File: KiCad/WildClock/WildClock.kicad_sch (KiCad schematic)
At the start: 35 parts, among them J1 UART, Q1 CA1, Q2 CA2, Q3 CA3, Q4 CA4, Q5 CAL, SW1 ButtonUp, SW2 ButtonDown, SW3 ButtonOK, U1 ESP32-C3-MINI-1, U2 LTC-4627JR, U3 74HC595

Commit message: make all clearer and neu pcb
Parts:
- R1, R15, R2, R3, R4, R5: value 1kOhm -> 1k
- R10, R11, R12, R13, R14, R7, R8, R9: value 150Ohm -> 150
- R16, R6: value 10kOhm -> 10k
- U2: value LTC-4627JR -> 7Segment
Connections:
- net +3.3V: now also BT1.1 (+), C1.2, C2.2, R15.2, U1.3 (3V3)
- net GND: now also BT1.2 (-), C1.1, C2.1, C3.1, U1.1 (GND), U1.2 (GND), U1.36 (GND), U1.37 (GND), U1.38 (GND), U1.39 (GND), U1.40 (GND), U1.41 (GND), U1.42 (GND), U1.43 (GND), U1.44 (GND), U1.45 (GND), U1.46 (GND), U1.47 (GND), U1.48 (GND), U1.49 (GND), U1.50 (GND), U1.51 (GND), U1.52 (GND), U1.53 (GND)
- net Q2: now reaches R2.1, U1.19 (GPIO5/ADC2_CH0)
- net BUZZ: now reaches BZ1.1 (-), U1.16 (GPIO10)
- net at R10.1: now also U2.3 (D); no longer U3.4 (QE)
- net at U2.5 (E): now also R11.1; no longer R10.2
- net CA1: now reaches Q1.3 (E), U2.1 (CA1)
- net at R7.1: now also U2.14 (A); no longer U3.7 (QH)
- net at U2.7 (DP): now also R14.1; no longer R7.2
- net at R13.1: now also U2.15 (G); no longer U3.1 (QB)
- net at U2.16 (B): now also R8.1; no longer R13.2
- net SWOK: now reaches R16.1, SW3.1, U1.5 (GPIO2/ADC1_CH2)
- net at U2.11 (F): now also R12.1; no longer R9.2
- net at U2.13 (C): now also R9.1; no longer R12.2
- net DP: now reaches R14.2
- net DP: now also U3.15 (QA); no longer U2.14 (A)
- net B: now reaches R8.2
- net B: now also U3.6 (QG); no longer U2.15 (G)
- net CA2: now reaches Q2.3 (E), U2.2 (CA2)
- net E: now reaches R11.2
- net E: now also U3.3 (QD); no longer U2.3 (D)
- net CAL: now reaches Q5.3 (E), U2.4 (CAL)
- net CA3: now reaches Q3.3 (E), U2.6 (CA3)
- net CA4: now reaches Q4.3 (E), U2.8 (CA4)
- net TXD0: now reaches J1.2 (Pin_2), U1.31 (GPIO21/U0TXD)
- net RXD0: now reaches J1.3 (Pin_3), U1.30 (GPIO20/U0RXD)
- net SRCLK: now reaches U1.27 (GPIO19/USB_D+), U3.11 (SRCLK)
- net RCLK: now reaches U1.26 (GPIO18/USB_D-), U3.12 (RCLK)
- net RCLK: no longer JP1.2 (B)
- net SER: now reaches U1.23 (GPIO9), U3.14 (SER)
- net SER: now also JP1.2 (B)
- net F: now reaches U3.2 (QC)
- net F: now also R12.2; no longer R12.1
- net C: now reaches U3.5 (QF)
- net C: now also R9.2; no longer R9.1
- net SWDOWN: now reaches SW2.1, U1.12 (GPIO0/ADC1_CH0/XTAL_32K_P)
- net SWUP: now reaches SW1.1, U1.13 (GPIO1/ADC1_CH1/XTAL_32K_N)
- net Q1: now reaches R1.1, U1.18 (GPIO4/ADC1_CH4)
- net Q3: now reaches R3.1
- net Q3: now also U1.21 (GPIO7); no longer U1.20 (GPIO6)
- net Q4: now reaches R4.1
- net Q4: now also R6.1, U1.22 (GPIO8); no longer U1.21 (GPIO7)
- net TILT: now reaches S1.2, U1.6 (GPIO3/ADC1_CH3)
- new net: C3.2, R15.1, U1.8 (EN/CHIP_PU)
- new net A: R7.2, U3.7 (QH)
- new net D: R10.2, U3.4 (QE)
- new net G: R13.2, U3.1 (QB)
- new net QL: R5.1, U1.20 (GPIO6)
- no-connect marks 0 -> 1
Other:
- note added: "7 Segment controll"
- note added: "Buttons"
- note added: "ESP Pinout"
- note added: "Interfaces"
- note added: "Output"
- note added: "Power Circuit"
- note added: "Sensor"
- moved on the sheet: BT1, BZ1, J1, JP1, Q1, Q2, Q3, Q4, Q5, S1, SW1, SW2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

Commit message: changed some footprints
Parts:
- removed Q1: CA1, Package_TO_SOT_THT:TO-92_Inline, symbol Transistor_BJT:BC547
- removed Q2: CA2, Package_TO_SOT_THT:TO-92_Inline, symbol Transistor_BJT:BC547
- removed Q3: CA3, Package_TO_SOT_THT:TO-92_Inline, symbol Transistor_BJT:BC547
- removed Q4: CA4, Package_TO_SOT_THT:TO-92_Inline, symbol Transistor_BJT:BC547
- removed Q5: CAL, Package_TO_SOT_THT:TO-92_Inline, symbol Transistor_BJT:BC547
- added Q1: CA1, Package_TO_SOT_SMD:SOT-23, symbol Transistor_BJT:MMBT3904
- added Q2: CA2, Package_TO_SOT_SMD:SOT-23, symbol Transistor_BJT:MMBT3904
- added Q3: CA3, Package_TO_SOT_SMD:SOT-23, symbol Transistor_BJT:MMBT3904
- added Q4: CA4, Package_TO_SOT_SMD:SOT-23, symbol Transistor_BJT:MMBT3904
- added Q5: CAL, Package_TO_SOT_SMD:SOT-23, symbol Transistor_BJT:MMBT3904
- SW1, SW2, SW3: footprint Button_Switch_THT:SW_PUSH_6mm -> Button_Switch_SMD:SW_Push_1P1T_NO_6x6mm_H9.5mm
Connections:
- net +3.3V: now also Q1.3 (C), Q2.3 (C), Q3.3 (C), Q4.3 (C), Q5.3 (C)
- net CA1: now also Q1.2 (E)
- net CA2: now also Q2.2 (E)
- net CA3: now also Q3.2 (E)
- net CA4: now also Q4.2 (E)
- net CAL: now also Q5.2 (E)
- net at R2.2: now also Q2.1 (B)
- net at R1.2: now also Q1.1 (B)
- net at R5.2: now also Q5.1 (B)
- net at R4.2: now also Q4.1 (B)
- net at R3.2: now also Q3.1 (B)
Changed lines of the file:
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@@
     (pin "2")
+  )
+  (symbol (lib_id "Transistor_BJT:MMBT3904") (at 31.75 104.14 270) (unit 1)
+    (in_bom yes) (on_board yes)
+    (property "Reference" "Q4" (id 0) (at 29.21 101.6 90))
+    (property "Value" "CA4" (id 1) (at 31.75 109.22 90))
+    (property "Footprint" "Package_TO_SOT_SMD:SOT-23" (id 2) (at 29.845 109.22 0)
+      (effects (font (size 1.27 1.27) italic) (justify left) hide)
+    )
+    (property "Datasheet" "https://www.onsemi.com/pub/Collateral/2N3903-D.PDF" (id 3) (at 31.75 104.14 0)
+      (effects (font (size 1.27 1.27)) (justify left) hide)
+    )
+    (pin "1")
+    (pin "2")
+    (pin "3")
   )
   (symbol (lib_id "power:GND") (at 153.67 107.95 90) (unit 1)
@@
     (pin "1")
   )
+  (symbol (lib_id "Transistor_BJT:MMBT3904") (at 31.75 63.5 270) (unit 1)
+    (in_bom yes) (on_board yes)
+    (property "Reference" "Q1" (id 0) (at 29.21 60.96 90))
+    (property "Value" "CA1" (id 1) (at 31.75 68.58 90))
+    (property "Footprint" "Package_TO_SOT_SMD:SOT-23" (id 2) (at 29.845 68.58 0)
+      (effects (font (size 1.27 1.27) italic) (justify left) hide)
+    )
+    (property "Datasheet" "https://www.onsemi.com/pub/Collateral/2N3903-D.PDF" (id 3) (at 31.75 63.5 0)
+      (effects (font (size 1.27 1.27)) (justify left) hide)
+    )
+    (pin "1")
+    (pin "2")
+    (pin "3")
+  )
   (symbol (lib_id "Device:Buzzer") (at 167.64 139.7 0) (mirror y) (unit 1)
     (in_bom yes) (on_board yes)
@@
     (pin "2")
   )
-  (symbol (lib_id "Transistor_BJT:BC547") (at 31.75 63.5 270) (unit 1)
-    (in_bom yes) (on_board yes)
-    (property "Reference" "Q1" (id 0) (at 29.21 60.96 90))
-    (property "Value" "CA1" (id 1) (at 31.75 68.58 90))
-    (property "Footprint" "Package_TO_SOT_THT:TO-92_Inline" (id 2) (at 29.845 68.58 0)
+  (symbol (lib_id "Transistor_BJT:MMBT3904") (at 31.75 116.84 270) (unit 1)
+    (in_bom yes) (on_board yes)
+    (property "Reference" "Q5" (id 0) (at 29.21 114.3 90))
+    (property "Value" "CAL" (id 1) (at 31.75 121.92 90))
+    (property "Footprint" "Package_TO_SOT_SMD:SOT-23" (id 2) (at 29.845 121.92 0)
       (effects (font (size 1.27 1.27) italic) (justify left) hide)
     )
-    (property "Datasheet" "https://www.onsemi.com/pub/Collateral/BC550-D.pdf" (id 3) (at 31.75 63.5 0)
+    (property "Datasheet" "https://www.onsemi.com/pub/Collateral/2N3903-D.PDF" (id 3) (at 31.75 116.84 0)
       (effects (font (size 1.27 1.27)) (justify left) hide)
     )
@@
     (property "Reference" "SW3" (id 0) (at 88.9 133.35 0))
     (property "Value" "ButtonOK" (id 1) (at 88.9 135.89 0))
-    (property "Footprint" "Button_Switch_THT:SW_PUSH_6mm" (id 2) (at 88.9 135.89 0)
+    (property "Footprint" "Button_Switch_SMD:SW_Push_1P1T_NO_6x6mm_H9.5mm" (id 2) (at 88.9 135.89 0)
       (effects (font (size 1.27 1.27)) hide)
     )
@@
     (pin "4")
   )
-  (symbol (lib_id "Transistor_BJT:BC547") (at 31.75 116.84 270) (unit 1)
-    (in_bom yes) (on_board yes)
-    (property "Reference" "Q5" (id 0) (at 29.21 114.3 90))
-    (property "Value" "CAL" (id 1) (at 31.75 121.92 90))
-    (property "Footprint" "Package_TO_SOT_THT:TO-92_Inline" (id 2) (at 29.845 121.92 0)
+  (symbol (lib_id "Transistor_BJT:MMBT3904") (at 31.75 91.44 270) (unit 1)
+    (in_bom yes) (on_board yes)
+    (property "Reference" "Q3" (id 0) (at 29.21 88.9 90))
+    (property "Value" "CA3" (id 1) (at 31.75 96.52 90))
+    (property "Footprint" "Package_TO_SOT_SMD:SOT-23" (id 2) (at 29.845 96.52 0)
       (effects (font (size 1.27 1.27) italic) (justify left) hide)
     )
-    (property "Datasheet" "https://www.onsemi.com/pub/Collateral/BC550-D.pdf" (id 3) (at 31.75 116.84 0)
+    (property "Datasheet" "https://www.onsemi.com/pub/Collateral/2N3903-D.PDF" (id 3) (at 31.75 91.44 0)
+      (effects (font (size 1.27 1.27)) (justify left) hide)
+    )
+    (pin "1")
+    (pin "2")
+    (pin "3")
+  )
+  (symbol (lib_id "Transistor_BJT:MMBT3904") (at 31.75 77.47 270) (unit 1)
+    (in_bom yes) (on_board yes)
+    (property "Reference" "Q2" (id 0) (at 29.21 74.93 90))
+    (property "Value" "CA2" (id 1) (at 31.75 82.55 90))
+    (property "Footprint" "Package_TO_SOT_SMD:SOT-23" (id 2) (at 29.845 82.55 0)
+      (effects (font (size 1.27 1.27) italic) (justify left) hide)
+    )
+    (property "Datasheet" "https://www.onsemi.com/pub/Collateral/2N3903-D.PDF" (id 3) (at 31.75 77.47 0)
       (effects (font (size 1.27 1.27)) (justify left) hide)
     )
@@
     (pin "2")
   )
-  (symbol (lib_id "Transistor_BJT:BC547") (at 31.75 91.44 270) (unit 1)
-    (in_bom yes) (on_board yes)
-    (property "Reference" "Q3" (id 0) (at 29.21 88.9 90))
-    (property "Value" "CA3" (id 1) (at 31.75 96.52 90))
-    (property "Footprint" "Package_TO_SOT_THT:TO-92_Inline" (id 2) (at 29.845 96.52 0)
-      (effects (font (size 1.27 1.27) italic) (justify left) hide)
-    )
-    (property "Datasheet" "https://www.onsemi.com/pub/Collateral/BC550-D.pdf" (id 3) (at 31.75 91.44 0)
-      (effects (font (size 1.27 1.27)) (justify left) hide)
-    )
-    (pin "1")
-    (pin "2")
-    (pin "3")
-  )
-  (symbol (lib_id "Transistor_BJT:BC547") (at 31.75 77.47 270) (unit 1)
-    (in_bom yes) (on_board yes)
-    (property "Reference" "Q2" (id 0) (at 29.21 74.93 90))
-    (property "Value" "CA2" (id 1) (at 31.75 82.55 90))
-    (property "Footprint" "Package_TO_SOT_THT:TO-92_Inline" (id 2) (at 29.845 82.55 0)
-      (effects (font (size 1.27 1.27) italic) (justify left) hide)
-    )
-    (property "Datasheet" "https://www.onsemi.com/pub/Collateral/BC550-D.pdf" (id 3) (at 31.75 77.47 0)
-      (effects (font (size 1.27 1.27)) (justify left) hide)
-    )
-    (pin "1")
-    (pin "2")
-    (pin "3")
-  )
   (symbol (lib_id "Device:R") (at 121.92 57.15 270) (unit 1)
     (in_bom yes) (on_board yes)
@@
     (pin "1")
   )
-  (symbol (lib_id "Transistor_BJT:BC547") (at 31.75 104.14 270) (unit 1)
-    (in_bom yes) (on_board yes)
-    (property "Reference" "Q4" (id 0) (at 29.21 101.6 90))
-    (property "Value" "CA4" (id 1) (at 31.75 109.22 90))
-    (property "Footprint" "Package_TO_SOT_THT:TO-92_Inline" (id 2) (at 29.845 109.22 0)
-      (effects (font (size 1.27 1.27) italic) (justify left) hide)
-    )
-    (property "Datasheet" "https://www.onsemi.com/pub/Collateral/BC550-D.pdf" (id 3) (at 31.75 104.14 0)
-      (effects (font (size 1.27 1.27)) (justify left) hide)
-    )
-    (pin "1")
-    (pin "2")
-    (pin "3")
-  )
   (symbol (lib_id "Switch:SW_Push") (at 27.94 140.97 0) (unit 1)
     (in_bom yes) (on_board yes)
     (property "Reference" "SW1" (id 0) (at 27.94 133.35 0))
     (property "Value" "ButtonUp" (id 1) (at 27.94 135.89 0))
-    (property "Footprint" "Button_Switch_THT:SW_PUSH_6mm" (id 2) (at 27.94 135.89 0)
+    (property "Footprint" "Button_Switch_SMD:SW_Push_1P1T_NO_6x6mm_H9.5mm" (id 2) (at 27.94 135.89 0)
       (effects (font (size 1.27 1.27)) hide)
     )
@@
     (property "Reference" "SW2" (id 0) (at 59.69 133.35 0))
     (property "Value" "ButtonDown" (id 1) (at 59.69 135.89 0))
-    (property "Footprint" "Button_Switch_THT:SW_PUSH_6mm" (id 2) (at 59.69 135.89 0)
+    (property "Footprint" "Button_Switch_SMD:SW_Push_1P1T_NO_6x6mm_H9.5mm" (id 2) (at 59.69 135.89 0)
       (effects (font (size 1.27 1.27)) hide)
     )
@@
       (reference "JP1") (unit 1) (value "Jumper_BOOT") (footprint "Connector_PinHeader_1.00mm:PinHeader_1x02_P1.00mm_Vertical")
     )
-    (path "/19149466-093f-494c-ad9e-63c53e92a41b"
-      (reference "Q1") (unit 1) (value "CA1") (footprint "Package_TO_SOT_THT:TO-92_Inline")
-    )
-    (path "/979b9bbf-6e1a-42d0-8fea-eb42374f2a80"
-      (reference "Q2") (unit 1) (value "CA2") (footprint "Package_TO_SOT_THT:TO-92_Inline")
-    )
-    (path "/8d0c18fa-e270-4d4a-a033-ec5a68a676e3"
-      (reference "Q3") (unit 1) (value "CA3") (footprint "Package_TO_SOT_THT:TO-92_Inline")
-    )
-    (path "/9ddf3c1f-7b3f-445c-8f18-ffb30090172f"
-      (reference "Q4") (unit 1) (value "CA4") (footprint "Package_TO_SOT_THT:TO-92_Inline")
-    )
-    (path "/4528a993-2673-4497-ae4f-06a4d5527096"
-      (reference "Q5") (unit 1) (value "CAL") (footprint "Package_TO_SOT_THT:TO-92_Inline")
+    (path "/076122f5-8a6d-41b4-9ff2-bda110edd813"
+      (reference "Q1") (unit 1) (value "CA1") (footprint "Package_TO_SOT_SMD:SOT-23")
+    )
+    (path "/44421386-2f43-4f34-ae8c-25366510c86b"
+      (reference "Q2") (unit 1) (value "CA2") (footprint "Package_TO_SOT_SMD:SOT-23")
+    )
+    (path "/3bbfdfa1-1f8e-4402-afb4-0c680a8663bf"
+      (reference "Q3") (unit 1) (value "CA3") (footprint "Package_TO_SOT_SMD:SOT-23")
+    )
+    (path "/0360746b-949e-4ad8-99c4-b4de53620631"
+      (reference "Q4") (unit 1) (value "CA4") (footprint "Package_TO_SOT_SMD:SOT-23")
+    )
+    (path "/161405ae-9068-4ac5-9c97-4db296fcbd48"
+      (reference "Q5") (unit 1) (value "CAL") (footprint "Package_TO_SOT_SMD:SOT-23")
     )
     (path "/f526df69-e0a2-4d6a-a448-2fc1af5fcd15"
@@
     )
     (path "/a0f7afd9-e1a0-4493-927b-f858c896c28f"
-      (reference "SW1") (unit 1) (value "ButtonUp") (footprint "Button_Switch_THT:SW_PUSH_6mm")
+      (reference "SW1") (unit 1) (value "ButtonUp") (footprint "Button_Switch_SMD:SW_Push_1P1T_NO_6x6mm_H9.5mm")
     )
     (path "/b1a991f1-4115-440b-91b7-23f9271c3989"
-      (reference "SW2") (unit 1) (value "ButtonDown") (footprint "Button_Switch_THT:SW_PUSH_6mm")
+      (reference "SW2") (unit 1) (value "ButtonDown") (footprint "Button_Switch_SMD:SW_Push_1P1T_NO_6x6mm_H9.5mm")
     )
     (path "/1eaec3da-e070-4c8f-a604-d4f168f6fdf4"
-      (reference "SW3") (unit 1) (value "ButtonOK") (footprint "Button_Switch_THT:SW_PUSH_6mm")
+      (reference "SW3") (unit 1) (value "ButtonOK") (footprint "Button_Switch_SMD:SW_Push_1P1T_NO_6x6mm_H9.5mm")
     )
     (path "/59553d1f-db58-4ebb-922c-4e1354cf99f4"

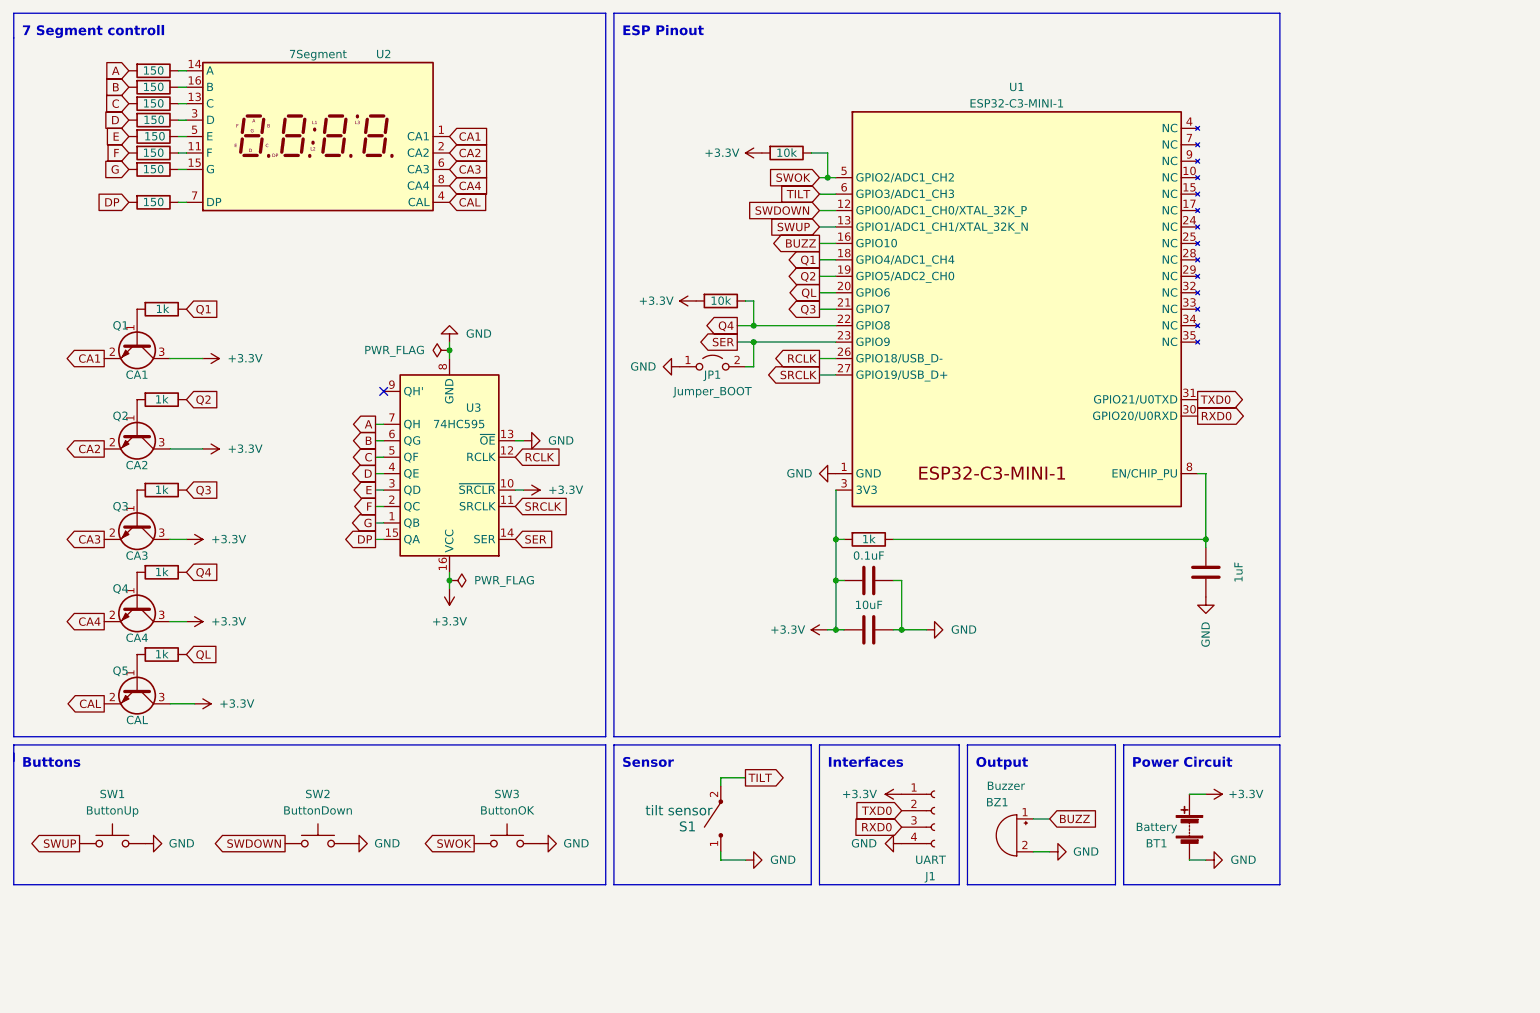
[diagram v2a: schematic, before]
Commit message: start updating footprints to match jlcpcb
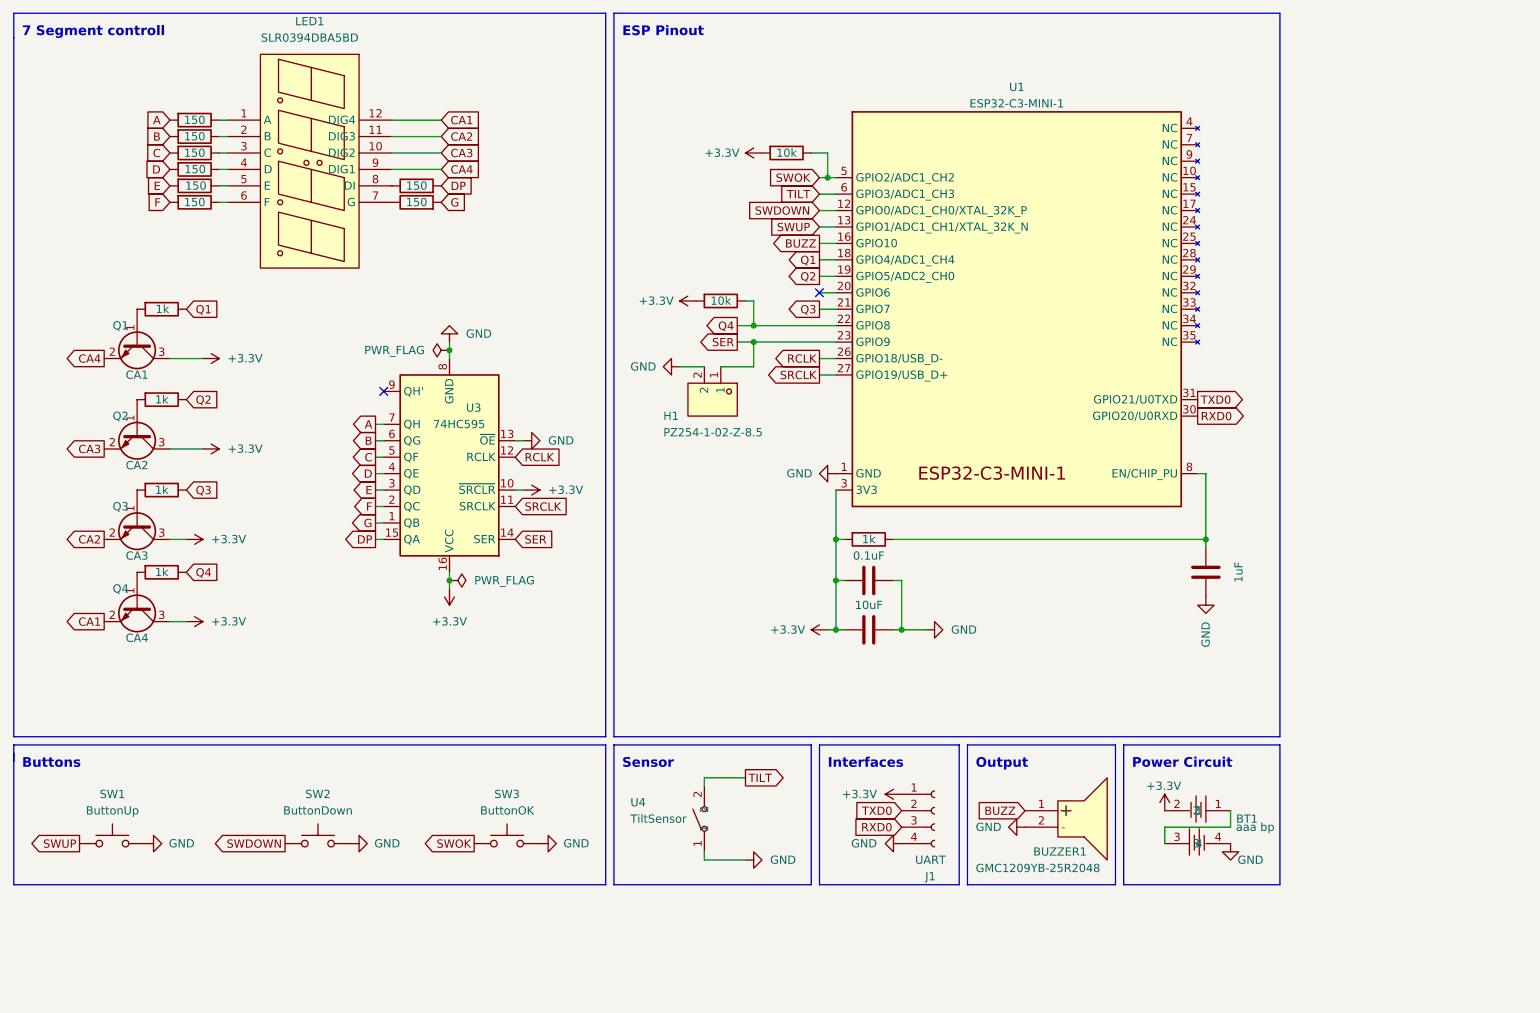
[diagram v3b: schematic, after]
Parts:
- removed BT1: Battery, Battery:BatteryHolder_Keystone_2462_2xAA, symbol Device:Battery
- removed BZ1: Buzzer, Buzzer_Beeper:Buzzer_12x9.5RM7.6, symbol Device:Buzzer
- removed JP1: Jumper_BOOT, Connector_PinHeader_1.00mm:PinHeader_1x02_P1.00mm_Vertical, symbol Jumper:Jumper_2_Open
- removed Q5: CAL, Package_TO_SOT_SMD:SOT-23, symbol Transistor_BJT:MMBT3904
- removed R5: 1k, Resistor_SMD:R_0805_2012Metric, symbol Device:R
- removed S1: tilt sensor, digikey-footprints:Tilt_Switch_RB-220-07A_R, symbol dk_Motion-Sensors-Tilt-Switches:RB-220-07A_R
- removed U2: 7Segment, Display_7Segment:LTC-4627Jx, symbol Display_Character:LTC-4627JR
- added BT1: aaa bp, easyeda2kicad:BAT-SMD_BH-AAA-B5AA001, symbol easyeda2kicad:BH-AAA-B5AA001
- added BUZZER1: GMC1209YB-25R2048, easyeda2kicad:BUZ-TH_BD12.0-P6.50-D0.6-FD, symbol easyeda2kicad:GMC1209YB-25R2048
- added H1: PZ254-1-02-Z-8.5, easyeda2kicad:HDR-TH_2P-P2.54-V-M, symbol easyeda2kicad:PZ254-1-02-Z-8.5
- added LED1: SLR0394DBA5BD, easyeda2kicad:LED-SEG-TH_SLR0394DBA5BD, symbol easyeda2kicad:SLR0394DBA5BD
- added U4: TiltSensor, easyeda2kicad:SENSOR-TH_SW-520DS-AB12G, symbol easyeda2kicad:SW-520DS-AB12G
- U3: footprint Package_SO:SOIC-16_3.9x9.9mm_P1.27mm -> easyeda2kicad:SOIC-16_L9.9-W3.9-P1.27-LS6.0-BL
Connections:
- net +3.3V: now also BT1.2
- net BUZZ: now also BUZZER1.1 (+)
- net CA1: now also Q4.2 (E), LED1.12 (DIG4); no longer Q1.2 (E)
- net CA2: now also Q3.2 (E), LED1.11 (DIG3); no longer Q2.2 (E)
- net CA3: now also Q2.2 (E), LED1.10 (DIG2); no longer Q3.2 (E)
- net CA4: now also Q1.2 (E), LED1.9 (DIG1); no longer Q4.2 (E)
- net GND: now also BT1.4, BUZZER1.2 (-), H1.2, U4.1
- net SER: now also H1.1
- net TILT: now also U4.2
- net at R10.1: now also LED1.4 (D)
- net at R7.1: now also LED1.1 (A)
- net at R13.1: now also LED1.7 (G)
- net at R12.1: now also LED1.6 (F)
- net at R9.1: now also LED1.3 (C)
- net at R8.1: now also LED1.2 (B)
- net at R11.1: now also LED1.5 (E)
- net at R14.1: now also LED1.8 (DI)
- net QL: no longer names the net of U1.20 (GPIO6)
- new net: BT1.1, BT1.3
- no-connect marks 1 -> 2
